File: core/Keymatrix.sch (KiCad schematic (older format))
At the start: 144 parts, among them K0 KEYSW, K1 KEYSW, K10 KEYSW, K11 KEYSW, K12 KEYSW, K13 KEYSW, K14 KEYSW, K15 KEYSW, K16 KEYSW, K17 KEYSW, K18 KEYSW, K19 KEYSW, K2 KEYSW, K20 KEYSW, K21 KEYSW, K22 KEYSW, K23 KEYSW, K24 KEYSW, K25 KEYSW, K26 KEYSW, K27 KEYSW, K28 KEYSW, K29 KEYSW, K3 KEYSW, K30 KEYSW, K31 KEYSW, K32 KEYSW, K33 KEYSW, K34 KEYSW, K35 KEYSW, K36 KEYSW, K37 KEYSW, K38 KEYSW, K39 KEYSW, K4 KEYSW, K40 KEYSW, K41 KEYSW, K42 KEYSW, K43 KEYSW, K44 KEYSW, K45 KEYSW, K46 KEYSW, K47 KEYSW, K48 KEYSW, K49 KEYSW, K5 KEYSW, K50 KEYSW, K51 KEYSW, K52 KEYSW, K53 KEYSW, K54 KEYSW, K55 KEYSW, K56 KEYSW, K57 KEYSW, K58 KEYSW, K59 KEYSW, K6 KEYSW, K60 KEYSW, K61 KEYSW, K62 KEYSW, K63 KEYSW, K64 KEYSW, K65 KEYSW, K66 KEYSW, K67 KEYSW, K68 KEYSW, K69 KEYSW, K7 KEYSW, K70 KEYSW, K71 KEYSW, K8 KEYSW, K9 KEYSW

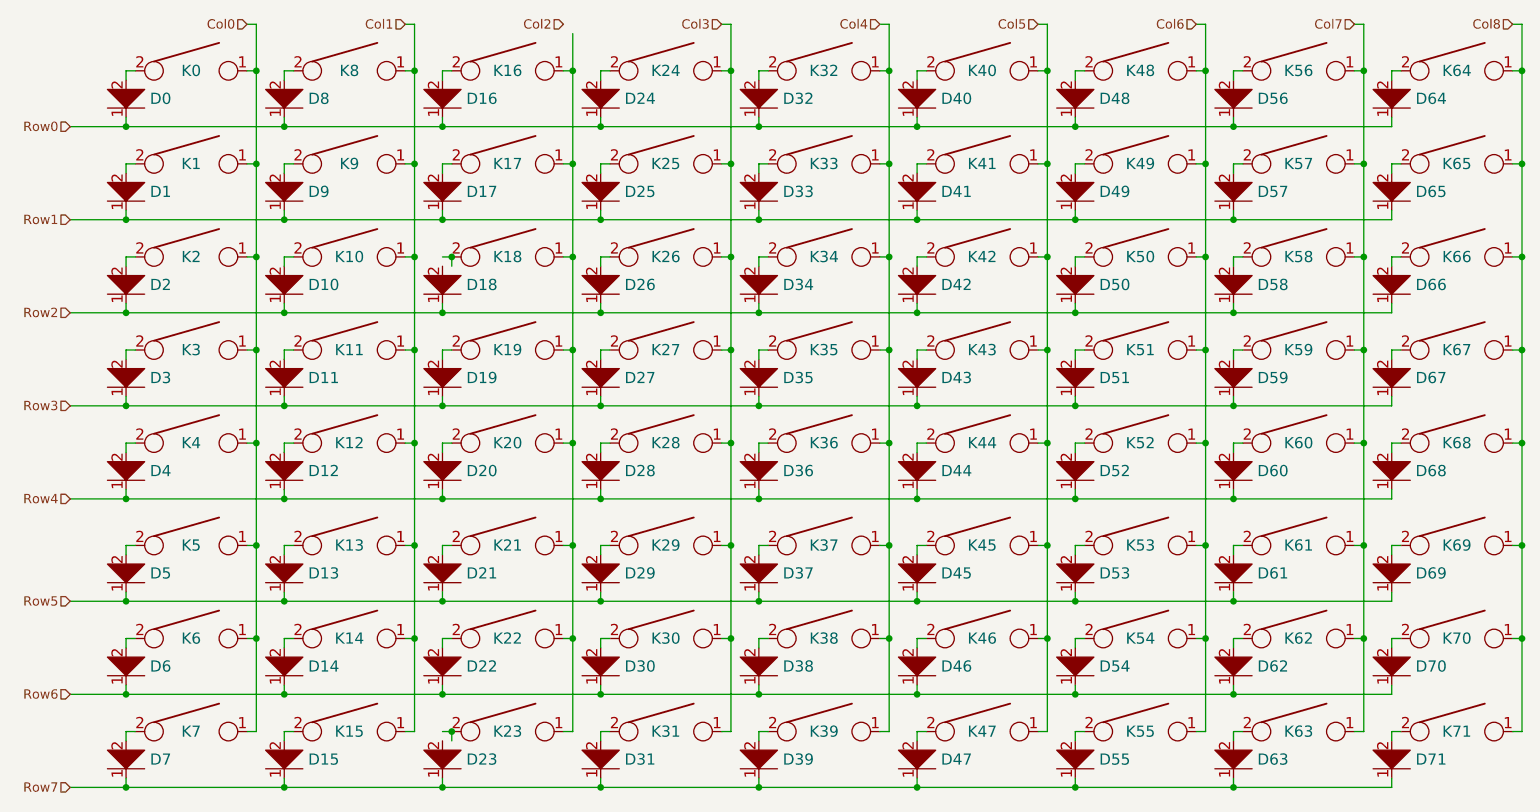
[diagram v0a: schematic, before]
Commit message: Fixed ERC errors and initially populated board
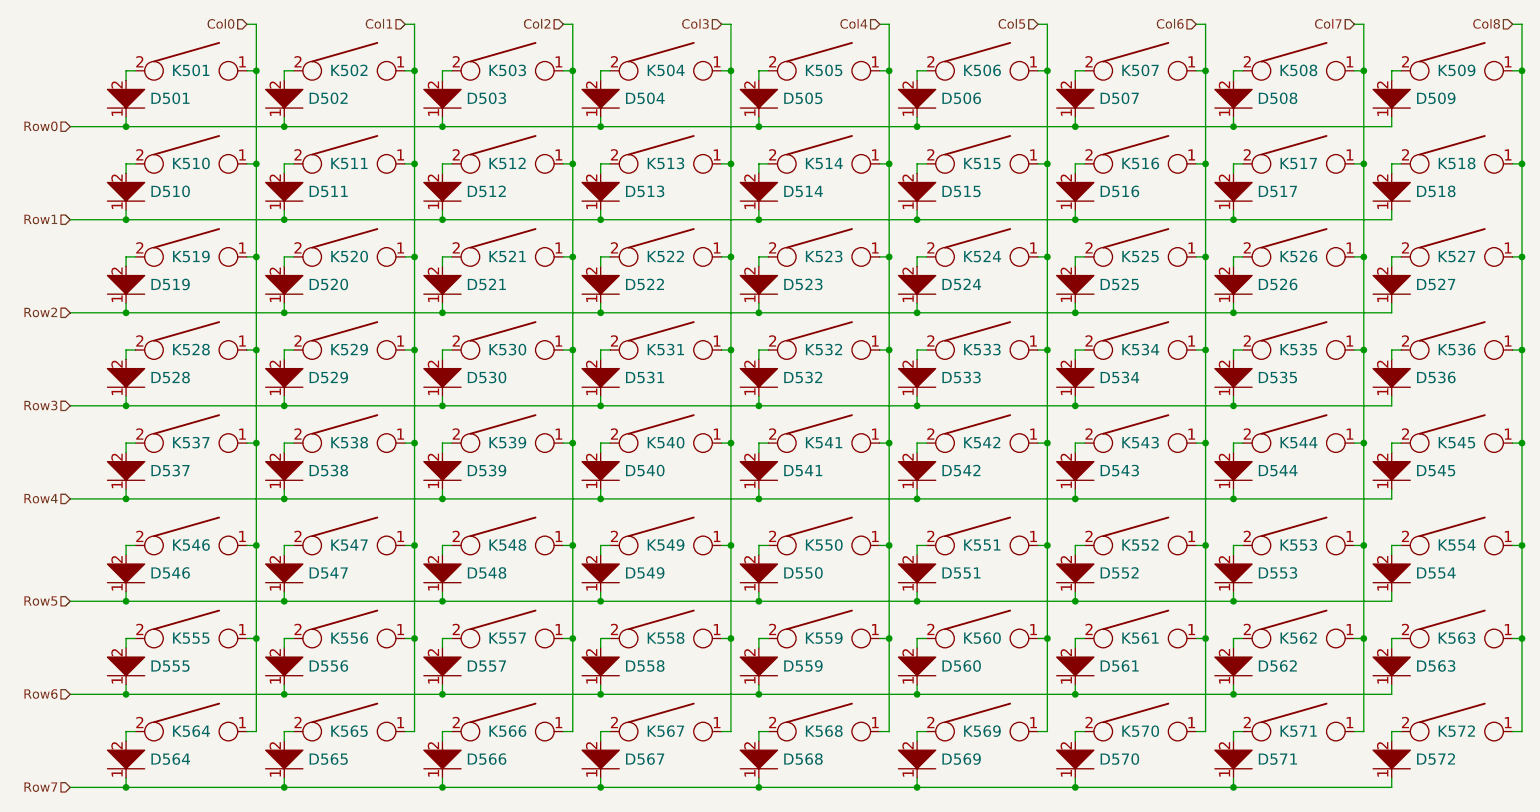
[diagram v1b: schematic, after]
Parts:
- renumbered D0 to D501, D8 to D502, D16 to D503, D24 to D504, D32 to D505, D40 to D506, D48 to D507, D56 to D508, D64 to D509, D1 to D510, D9 to D511, D17 to D512, D25 to D513, D33 to D514, D41 to D515, D49 to D516, D57 to D517, D65 to D518, D2 to D519, D10 to D520, D18 to D521, D26 to D522, D34 to D523, D42 to D524, D50 to D525, D58 to D526, D66 to D527, D3 to D528, D11 to D529, D19 to D530, D27 to D531, D35 to D532, D43 to D533, D51 to D534, D59 to D535, D67 to D536, D4 to D537, D12 to D538, D20 to D539, D28 to D540, D36 to D541, D44 to D542, D52 to D543, D60 to D544, D68 to D545, D5 to D546, D13 to D547, D21 to D548, D29 to D549, D37 to D550, D45 to D551, D53 to D552, D61 to D553, D69 to D554, D6 to D555, D14 to D556, D22 to D557, D30 to D558, D38 to D559, D46 to D560, D54 to D561, D62 to D562, D70 to D563, D7 to D564, D15 to D565, D23 to D566, D31 to D567, D39 to D568, D47 to D569, D55 to D570, D63 to D571, D71 to D572, K0 to K501, K8 to K502, K16 to K503, K24 to K504, K32 to K505, K40 to K506, K48 to K507, K56 to K508, K64 to K509, K1 to K510, K9 to K511, K17 to K512, K25 to K513, K33 to K514, K41 to K515, K49 to K516, K57 to K517, K65 to K518, K2 to K519, K10 to K520, K18 to K521, K26 to K522, K34 to K523, K42 to K524, K50 to K525, K58 to K526, K66 to K527, K3 to K528, K11 to K529, K19 to K530, K27 to K531, K35 to K532, K43 to K533, K51 to K534, K59 to K535, K67 to K536, K4 to K537, K12 to K538, K20 to K539, K28 to K540, K36 to K541, K44 to K542, K52 to K543, K60 to K544, K68 to K545, K5 to K546, K13 to K547, K21 to K548, K29 to K549, K37 to K550, K45 to K551, K53 to K552, K61 to K553, K69 to K554, K6 to K555, K14 to K556, K22 to K557, K30 to K558, K38 to K559, K46 to K560, K54 to K561, K62 to K562, K70 to K563, K7 to K564, K15 to K565, K23 to K566, K31 to K567, K39 to K568, K47 to K569, K55 to K570, K63 to K571, K71 to K572
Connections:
- net Col2: now also K503.1, K512.1, K521.1, K530.1, K539.1, K548.1, K557.1, K566.1
- net at D521.2: now also K521.2
- net at D566.2: now also K566.2
